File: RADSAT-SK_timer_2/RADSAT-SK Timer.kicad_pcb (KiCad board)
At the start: 2 copper layers, 90.2 x 95.9 mm, 125 parts, among them J101 Conn_02x26_Odd_Even, J103 Conn_02x26_Odd_Even, J201 Conn_01x07, J202 Conn_01x05, J203 Conn_01x03, J204 Conn_01x02, J205 Conn_01x02, J206 Conn_01x02, Q101 IRLML2060, Q102 IRLML2060, Q103 IRLML2060, Q104 IRLML2060, Q105 IRLML2060, Q106 IRLML2060, Q107 IRLML2060, Q108 IRLML2060, Q109 IRLML2060, Q201 IRLML2060, Q202 IRLML2060, Q204 IRLML2060, Q205 IRLML2060, Q206 IRLML2060, Q207 IRLML2060, SW201 SW_Push, SW202 SW_Push, SW203 SW_Push, SW204 SW_Push, SW205 SW_Push, SW206 SW_Push, U101 LM397MF, U102 LM397MF, U103 LM397MF, U104 CD4052B, U202 LTC3440EMSPBF, U230 CPC1117N, U240 CPC1117N, U250 CPC1117N, U260 CPC1117N

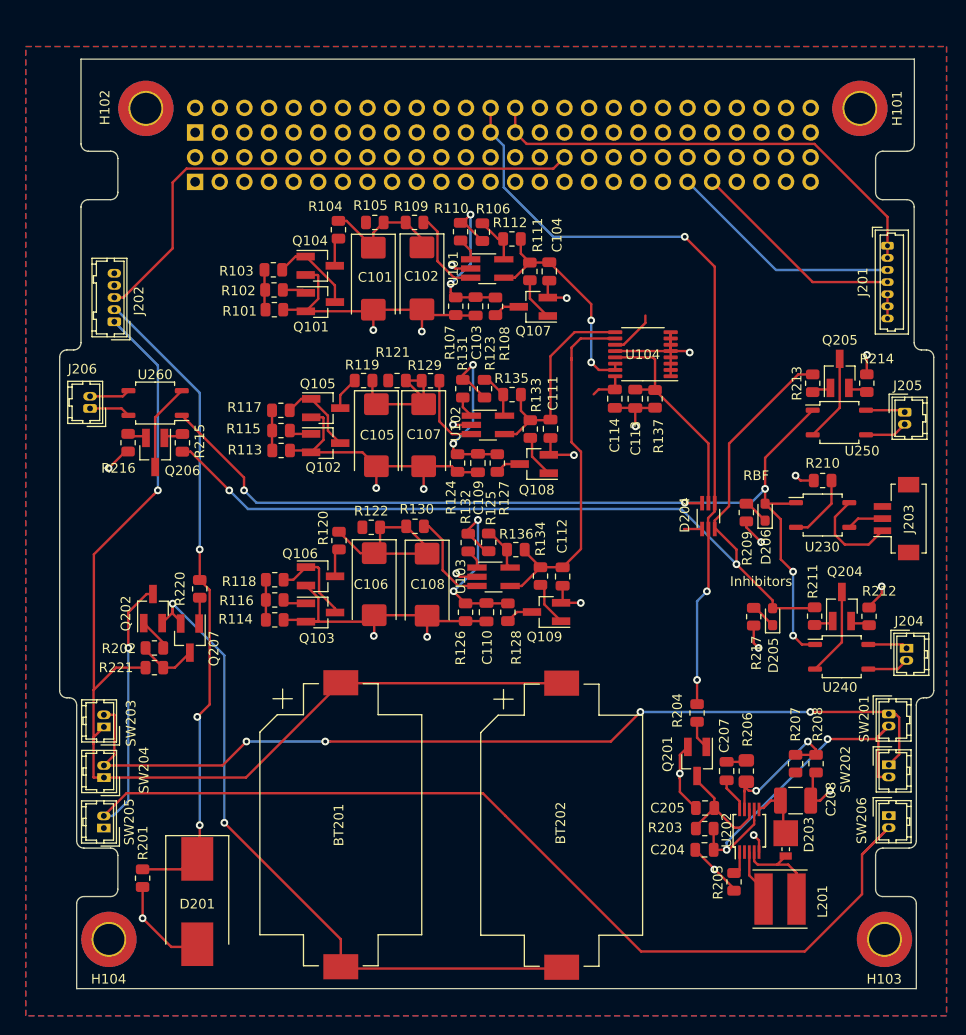
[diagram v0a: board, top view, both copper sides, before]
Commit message: Tracing and PCB design for the new TMIB rev 1
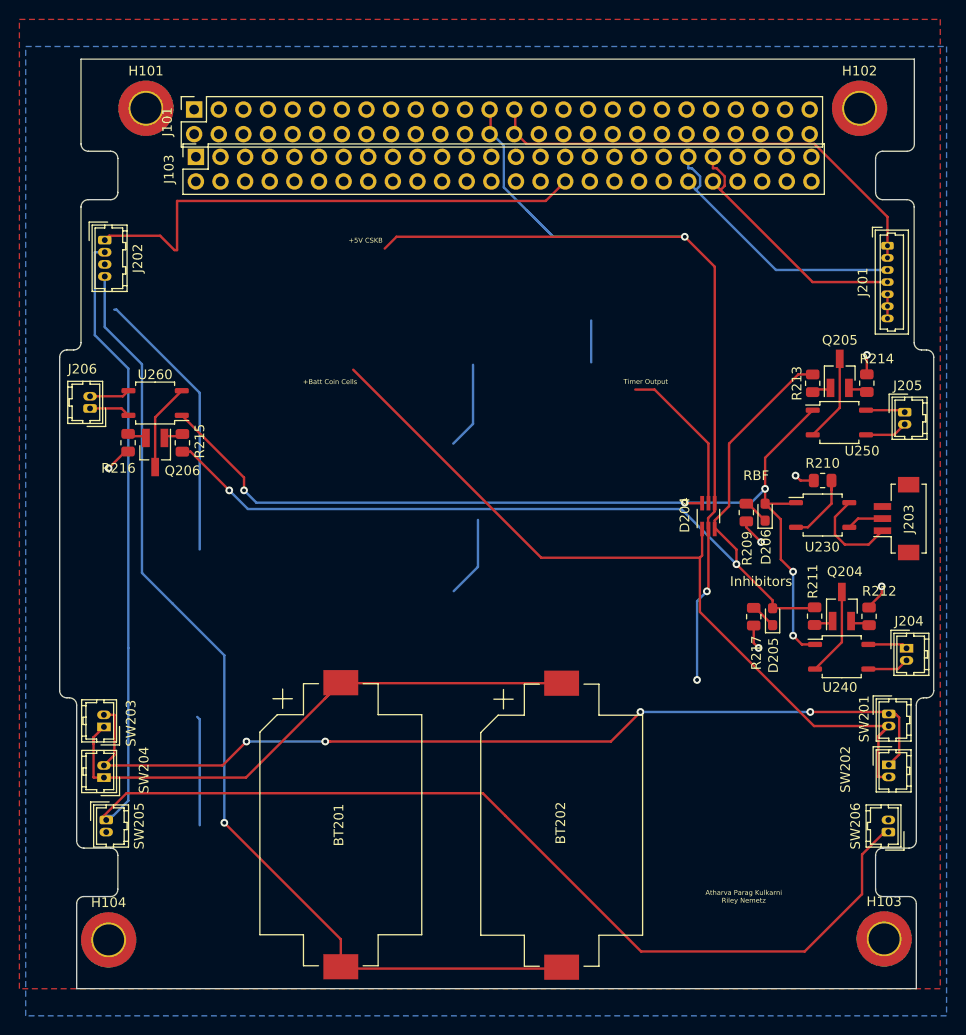
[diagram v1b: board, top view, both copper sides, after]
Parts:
- removed C101, C102, C105, C106, C107, C108: 330u, Capacitor_Tantalum_SMD:CP_EIA-7343-30_AVX-N_Pad2.25x2.55mm_HandSolder
- removed C103, C104, C109, C110, C111, C112, C113, C114: 100n, Capacitor_SMD:C_0805_2012Metric
- removed C204: 10uF, Capacitor_SMD:C_0805_2012Metric
- removed C205: 0.1uF, Capacitor_SMD:C_0805_2012Metric
- removed C207: 1.5nF, Capacitor_SMD:C_0805_2012Metric
- removed C208: 22uF, Capacitor_SMD:C_1210_3225Metric_Pad1.33x2.70mm_HandSolder
- removed D201: 5.0SMDJ5.0A, Diode_SMD:D_SMC_Handsoldering
- removed D203: MBRM120LT3G, Diode_SMD:D_Powermite_AK
- removed G***: LOGO, USSTlogo:USSTLOGO
- removed L201: 10uH, Sumida_inductor:Sumida_inductor
- removed Q101, Q102, Q103, Q104, Q105, Q106, Q107, Q108, Q109, Q201, Q202, Q207: IRLML2060, Package_TO_SOT_SMD:SOT-23_Handsoldering
- removed R101, R103, R107, R113, R114, R117, R118, R124, R126, R203, R221: 1M, Resistor_SMD:R_0805_2012Metric
- removed R102, R111, R115, R116, R133, R134, R202, R204, R220: 100, Resistor_SMD:R_0805_2012Metric
- removed R104, R119, R120: 1K, Resistor_SMD:R_0805_2012Metric
- removed R105, R121, R122: 3.48M, Resistor_SMD:R_0805_2012Metric
- removed R106, R123, R125: 442K, Resistor_SMD:R_0805_2012Metric
- removed R108, R109, R110, R112, R127, R128, R129, R130, R131, R132, R135, R136: 1k, Resistor_SMD:R_0805_2012Metric
- removed R137: 5.1M, Resistor_SMD:R_0805_2012Metric
- removed R201: 3M, Resistor_SMD:R_0805_2012Metric
- removed R205: 60.4K, Resistor_SMD:R_0805_2012Metric
- removed R206: 15k, Resistor_SMD:R_0805_2012Metric
- removed R207: 619k, Resistor_SMD:R_0805_2012Metric
- removed R208: 200k, Resistor_SMD:R_0805_2012Metric
- removed U101, U102, U103: LM397MF, Package_TO_SOT_SMD:TSOT-23-5_HandSoldering
- removed U104: CD4052B, Package_SO:TSSOP-16_4.4x5mm_P0.65mm
- removed U202: LTC3440EMSPBF, Package_SO:MSOP-10_3x3mm_P0.5mm
- J101, J103: moved to F.Cu
- J202: value Conn_01x05 -> Conn_01x04_Female; footprint Connector_Hirose:Hirose_DF13-05P-1.25DSA_1x05_P1.25mm_Vertical -> Connector_Hirose:Hirose_DF13-04P-1.25DSA_1x04_P1.25mm_Vertical
- U230, U240, U250, U260: value CPC1117N -> CPC1114N
- moved H101 73.7 mm to (43.7, 55.1), turned to 0 degrees
- moved H102 73.6 mm to (117.3, 55.1), turned to 0 degrees
- moved J202 8.48 mm to (39.5, 68.7), turned to 270 degrees
- moved J103 2.58 mm to (48.9, 60.1), turned to 90 degrees
- moved J101 2.37 mm to (48.7, 55.2), turned to 90 degrees
- moved SW206 1.70 mm to (120.3, 129.7), turned to 90 degrees
- moved SW205 0.87 mm to (39.6, 128.5), turned to 270 degrees
- moved H103 0.06 mm to (119.9, 140.8), turned to 0 degrees
- moved H104 0.06 mm to (39.9, 140.9), turned to 0 degrees
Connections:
- J101 pad 1: (no net) -> Net-(J101-Pad1)
- J101 pad 10: (no net) -> Net-(J101-Pad10)
- J101 pad 11: (no net) -> Net-(J101-Pad11)
- J101 pad 12: (no net) -> Net-(J101-Pad12)
- J101 pad 13: (no net) -> Net-(J101-Pad13)
- J101 pad 14: (no net) -> Net-(J101-Pad14)
- J101 pad 15: (no net) -> Net-(J101-Pad15)
- J101 pad 16: (no net) -> Net-(J101-Pad16)
- J101 pad 17: (no net) -> Net-(J101-Pad17)
- J101 pad 18: (no net) -> Net-(J101-Pad18)
- J101 pad 19: (no net) -> Net-(J101-Pad19)
- J101 pad 2: (no net) -> Net-(J101-Pad2)
- J101 pad 20: (no net) -> Net-(J101-Pad20)
- J101 pad 21: (no net) -> Net-(J101-Pad21)
- J101 pad 22: (no net) -> Net-(J101-Pad22)
- J101 pad 23: (no net) -> Net-(J101-Pad23)
- J101 pad 24: (no net) -> Net-(J101-Pad24)
- J101 pad 3: (no net) -> Net-(J101-Pad3)
- J101 pad 31: (no net) -> Net-(J101-Pad31)
- J101 pad 33: (no net) -> Net-(J101-Pad33)
- J101 pad 34: (no net) -> Net-(J101-Pad34)
- J101 pad 35: (no net) -> Net-(J101-Pad35)
- J101 pad 36: (no net) -> Net-(J101-Pad36)
- J101 pad 37: (no net) -> Net-(J101-Pad37)
- J101 pad 38: (no net) -> Net-(J101-Pad38)
- J101 pad 39: (no net) -> Net-(J101-Pad39)
- J101 pad 4: (no net) -> Net-(J101-Pad4)
- J101 pad 40: (no net) -> Net-(J101-Pad40)
- J101 pad 41: (no net) -> Net-(J101-Pad41)
- J101 pad 42: (no net) -> Net-(J101-Pad42)
- J101 pad 43: (no net) -> Net-(J101-Pad43)
- J101 pad 44: (no net) -> Net-(J101-Pad44)
- J101 pad 45: (no net) -> Net-(J101-Pad45)
- J101 pad 46: (no net) -> Net-(J101-Pad46)
- J101 pad 47: (no net) -> Net-(J101-Pad47)
- J101 pad 48: (no net) -> Net-(J101-Pad48)
- J101 pad 49: (no net) -> Net-(J101-Pad49)
- J101 pad 5: (no net) -> Net-(J101-Pad5)
- J101 pad 50: (no net) -> Net-(J101-Pad50)
- J101 pad 51: (no net) -> Net-(J101-Pad51)
- J101 pad 52: (no net) -> Net-(J101-Pad52)
- J101 pad 6: (no net) -> Net-(J101-Pad6)
- J101 pad 7: (no net) -> Net-(J101-Pad7)
- J101 pad 8: (no net) -> Net-(J101-Pad8)
- J101 pad 9: (no net) -> Net-(J101-Pad9)
- J103 pad 1: (no net) -> Net-(J103-Pad1)
- J103 pad 10: (no net) -> Net-(J103-Pad10)
- J103 pad 11: (no net) -> Net-(J103-Pad11)
- J103 pad 12: (no net) -> Net-(J103-Pad12)
- J103 pad 13: (no net) -> Net-(J103-Pad13)
- J103 pad 14: (no net) -> Net-(J103-Pad14)
- J103 pad 15: (no net) -> Net-(J103-Pad15)
- J103 pad 16: (no net) -> Net-(J103-Pad16)
- J103 pad 17: (no net) -> Net-(J103-Pad17)
- J103 pad 18: (no net) -> Net-(J103-Pad18)
- J103 pad 19: (no net) -> Net-(J103-Pad19)
- J103 pad 2: (no net) -> Net-(J103-Pad2)
- J103 pad 20: (no net) -> Net-(J103-Pad20)
- J103 pad 21: (no net) -> Net-(J103-Pad21)
- J103 pad 22: (no net) -> Net-(J103-Pad22)
- J103 pad 23: (no net) -> Net-(J103-Pad23)
- J103 pad 24: (no net) -> Net-(J103-Pad24)
- J103 pad 25: (no net) -> Net-(J103-Pad25)
- J103 pad 26: (no net) -> Net-(J103-Pad26)
- J103 pad 27: (no net) -> Net-(J103-Pad27)
- J103 pad 28: (no net) -> Net-(J103-Pad28)
- J103 pad 29: (no net) -> Net-(J103-Pad29)
- J103 pad 3: (no net) -> Net-(J103-Pad3)
- J103 pad 30: (no net) -> Net-(J103-Pad30)
- J103 pad 31: (no net) -> Net-(J103-Pad31)
- J103 pad 33: (no net) -> Net-(J103-Pad33)
- J103 pad 34: (no net) -> Net-(J103-Pad34)
- J103 pad 35: (no net) -> Net-(J103-Pad35)
- J103 pad 36: (no net) -> Net-(J103-Pad36)
- J103 pad 37: (no net) -> Net-(J103-Pad37)
- J103 pad 38: (no net) -> Net-(J103-Pad38)
- J103 pad 39: (no net) -> Net-(J103-Pad39)
- J103 pad 4: (no net) -> Net-(J103-Pad4)
- J103 pad 40: (no net) -> Net-(J103-Pad40)
- J103 pad 42: (no net) -> Net-(J103-Pad42)
- J103 pad 44: (no net) -> Net-(J103-Pad44)
- J103 pad 45: (no net) -> Net-(J103-Pad45)
- J103 pad 46: (no net) -> Net-(J103-Pad46)
- J103 pad 47: (no net) -> Net-(J103-Pad47)
- J103 pad 48: (no net) -> Net-(J103-Pad48)
- J103 pad 49: (no net) -> Net-(J103-Pad49)
- J103 pad 5: (no net) -> Net-(J103-Pad5)
- J103 pad 50: (no net) -> Net-(J103-Pad50)
- J103 pad 51: (no net) -> Net-(J103-Pad51)
- J103 pad 52: (no net) -> Net-(J103-Pad52)
- J103 pad 6: (no net) -> Net-(J103-Pad6)
- J103 pad 7: (no net) -> Net-(J103-Pad7)
- J103 pad 8: (no net) -> Net-(J103-Pad8)
- J103 pad 9: (no net) -> Net-(J103-Pad9)
- J202 pad 1: Net-(BT201-Pad1) -> USB_Charge
- J202 pad 2: Net-(D201-Pad1) -> Net-(J202-Pad2)
- J202 pad 3: USB_Charge -> GND
- J202 pad 4: GND -> Net-(BT201-Pad2)
- J203 pad 3: (no net) -> Net-(J203-Pad3)
- SW201 pad 2: Net-(C204-Pad1) -> +BATT
- SW202 pad 2: Net-(C204-Pad1) -> +BATT
- SW205 pad 1: GND -> Net-(J202-Pad2)
- SW205 pad 2: Net-(Q202-Pad3) -> GND
- SW206 pad 1: GND -> Net-(J202-Pad2)
- SW206 pad 2: Net-(Q202-Pad3) -> GND
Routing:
- net Net-(J202-Pad2): track 0.00 -> 159.8 mm
- net Net-(Q202-Pad3): track 126.2 -> 0.00 mm, vias 1 -> 0
- net GND: track 179.1 -> 79.0 mm, vias 25 -> 6
- net Net-(D201-Pad1): track 66.9 -> 0.00 mm, vias 3 -> 0
- net Net-(BT201-Pad1): track 112.7 -> 60.8 mm, vias 1 -> 0
- net +BATT: track 43.4 -> 85.4 mm
- net Net-(C204-Pad1): track 38.5 -> 0.00 mm, vias 2 -> 0
- net Timer_C_out: track 38.3 -> 0.00 mm
- net +5V: track 79.8 -> 114.9 mm
- net Net-(BT201-Pad2): track 73.3 -> 106.0 mm, vias 2 -> 1
- net Timer_A_out: track 23.8 -> 0.00 mm, vias 2 -> 0
- net Timer_B_out: track 22.6 -> 0.00 mm
- net Net-(C106-Pad1): track 19.4 -> 0.00 mm
- net Net-(C109-Pad1): track 19.3 -> 0.00 mm, vias 2 -> 0
- net Net-(C110-Pad1): track 19.2 -> 0.00 mm, vias 2 -> 0
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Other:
- board text added: "+5V CSKB"
- board text added: "+Batt Coin Cells"
- board text added: "Atharva Parag Kulkarni Riley Nemetz"
- board text added: "Timer Output"
